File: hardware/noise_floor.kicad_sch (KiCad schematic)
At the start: 14 parts, among them J1 DC Power, J10 IO/Switch Connector 2 (Switch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, J11 Battery, J2 Input, J3 Output, J6 IO/Effect Connector 1 (IO Sid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, J7 IO/Switch Connector 1 (IO Sid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, J8 IO/Switch Connector 2 (IO Sid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, J9 IO/Switch Connector 1 (Switch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, SW1 Footswitch

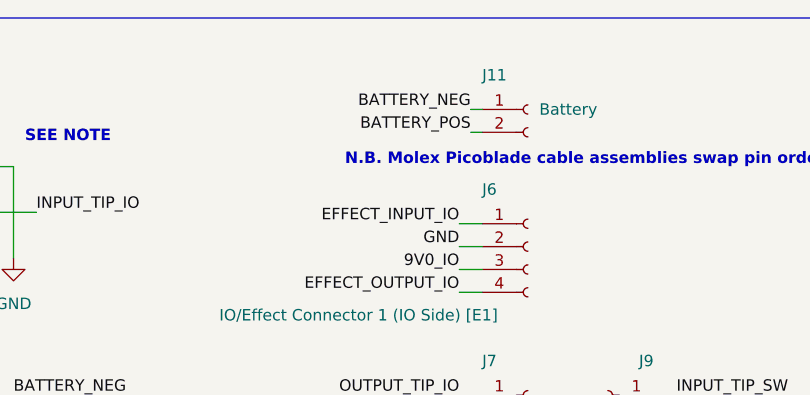
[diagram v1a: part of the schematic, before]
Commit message: Fix one issue discovered in testing of v0.2 hardware
 - swap nets on battery JST connector
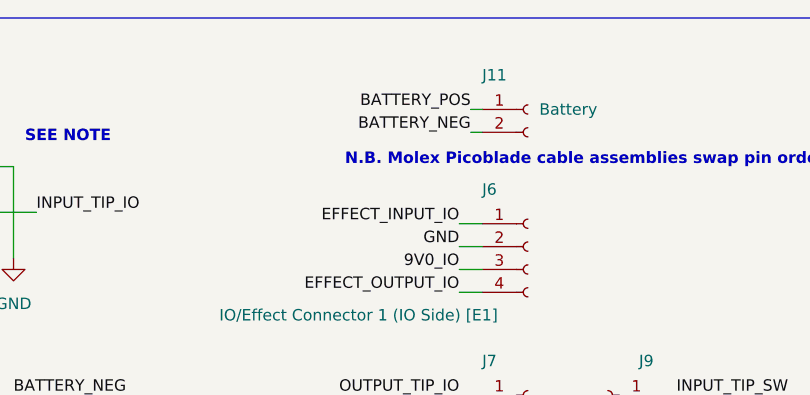
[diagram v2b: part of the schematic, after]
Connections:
- net BATTERY_NEG: now also J11.2 (Pin_2); no longer J11.1 (Pin_1)
- net BATTERY_POS: now also J11.1 (Pin_1); no longer J11.2 (Pin_2)
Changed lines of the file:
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@@
   (title_block
     (title "Noise Floor Interface Boards")
-    (date "2023-03-16")
-    (rev "v0.2")
+    (date "2023-03-23")
+    (rev "v0.21")
     (comment 1 "github.com/whbeers/noise_floor")
   )
@@
     (effects (font (size 1.27 1.27)) (justify left bottom))
   )
-  (label "BATTERY_POS" (at 85.09 26.67 180) (fields_autoplaced)
+  (label "BATTERY_NEG" (at 85.09 26.67 180) (fields_autoplaced)
     (effects (font (size 1.27 1.27)) (justify right bottom))
   )
-  (label "BATTERY_NEG" (at 85.09 24.13 180) (fields_autoplaced)
+  (label "BATTERY_POS" (at 85.09 24.13 180) (fields_autoplaced)
     (effects (font (size 1.27 1.27)) (justify right bottom))
   )

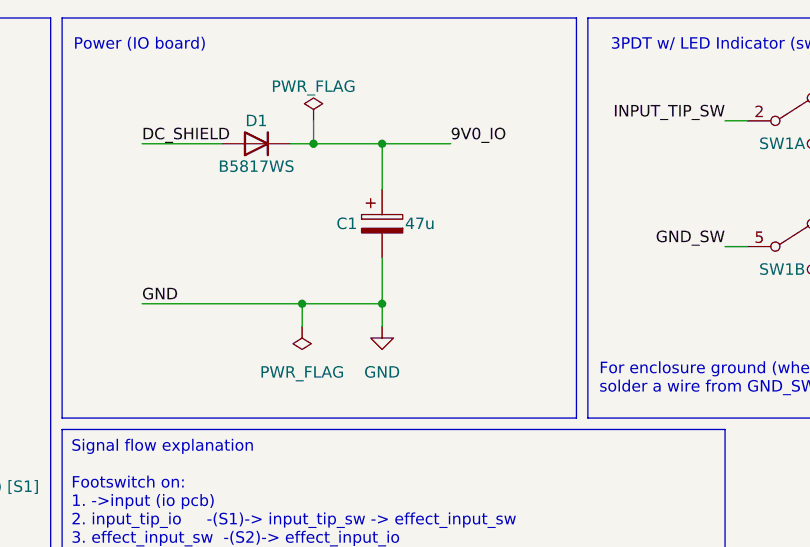
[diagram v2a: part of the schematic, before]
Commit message: improve power filtering and move to more SMD components
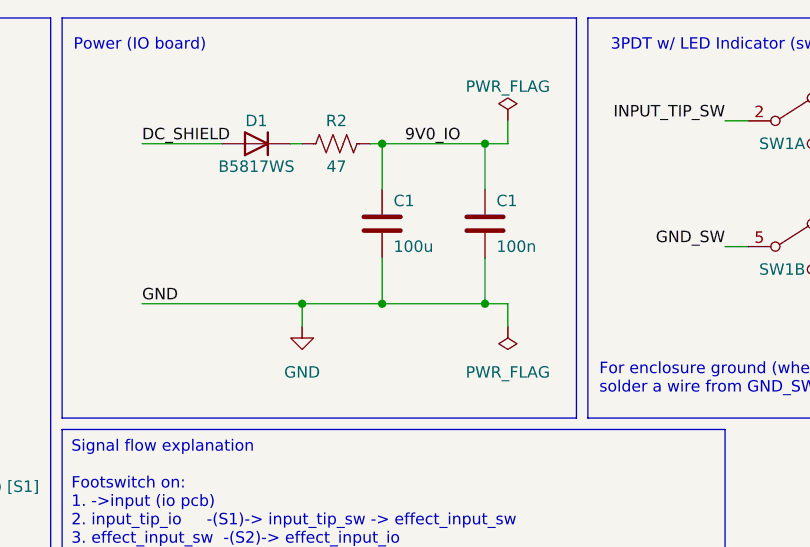
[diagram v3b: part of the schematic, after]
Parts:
- added C1: 100n, Capacitor_SMD:C_1206_3216Metric, symbol Device:C
- added R2: 47, Resistor_SMD:R_1206_3216Metric_Pad1.30x1.75mm_HandSolder, symbol Device:R_US
- C1: value 47u -> 100u; footprint Capacitor_THT:CP_Radial_D5.0mm_P2.50mm -> Capacitor_SMD:CP_Elec_6.3x7.7; symbol Device:C_Polarized -> Device:C
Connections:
- net 9V0_IO: now also C1.1, R2.1; no longer D1.1 (K)
- net GND: now also C1.2
- new net: D1.1 (K), R2.2

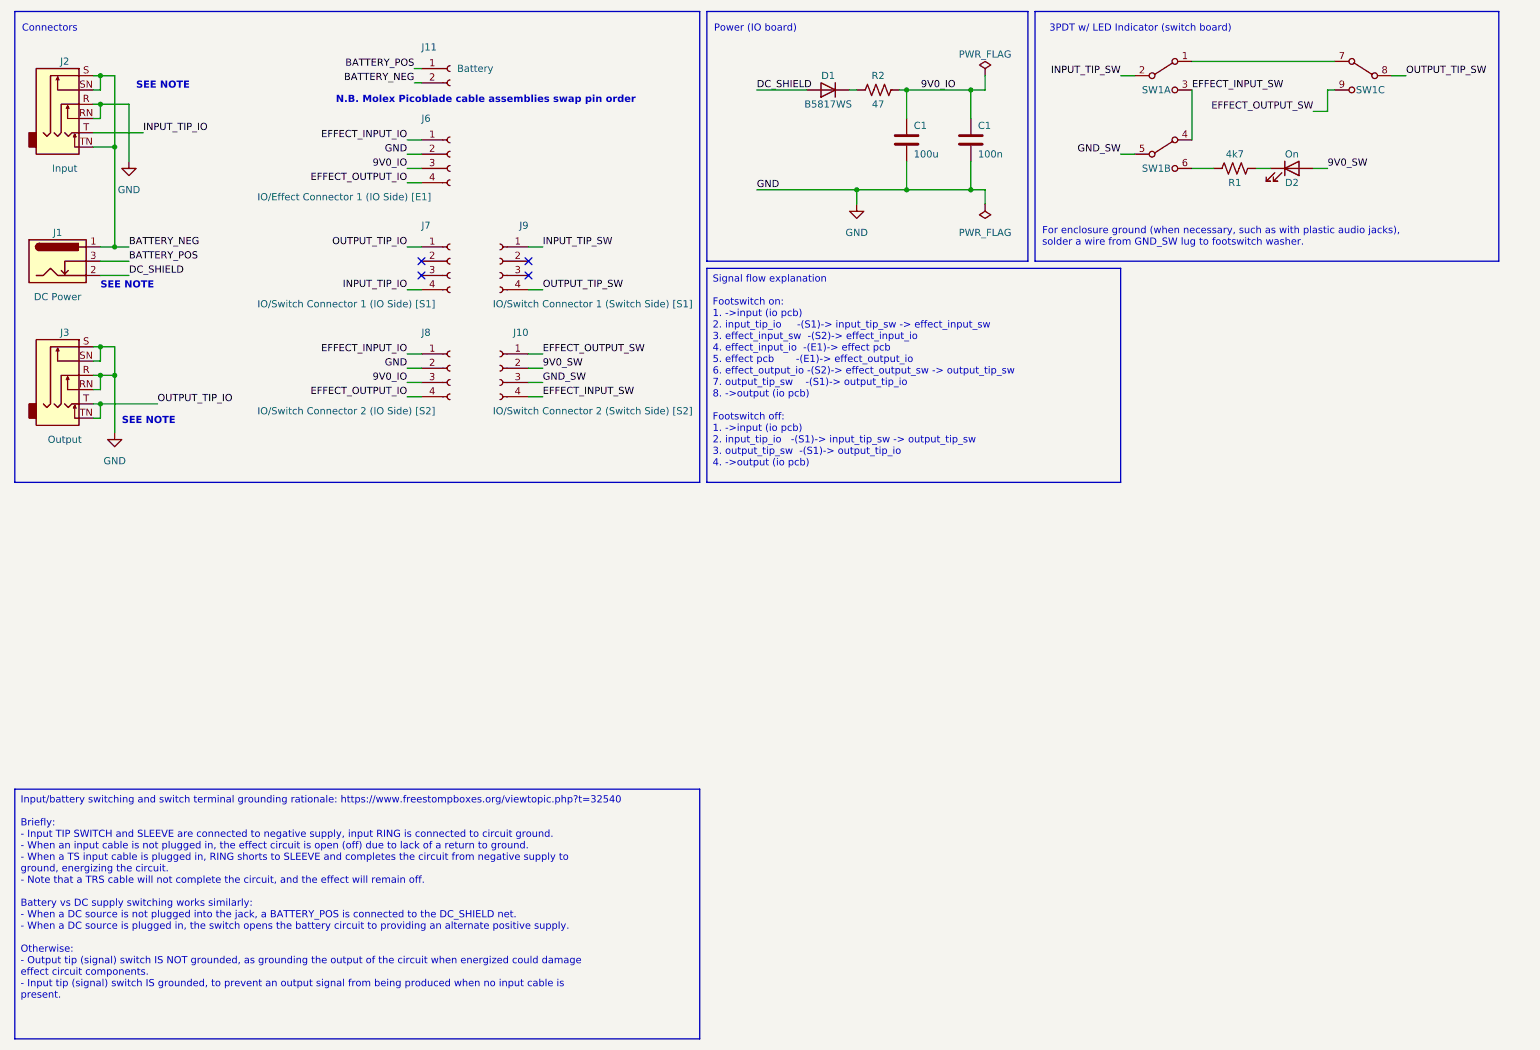
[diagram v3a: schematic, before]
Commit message: v0.30 includes a new "ux" board, with the initial feature set:
 - board-to-board connector interface for expandability
 - three potentiometers and three SPDT switches
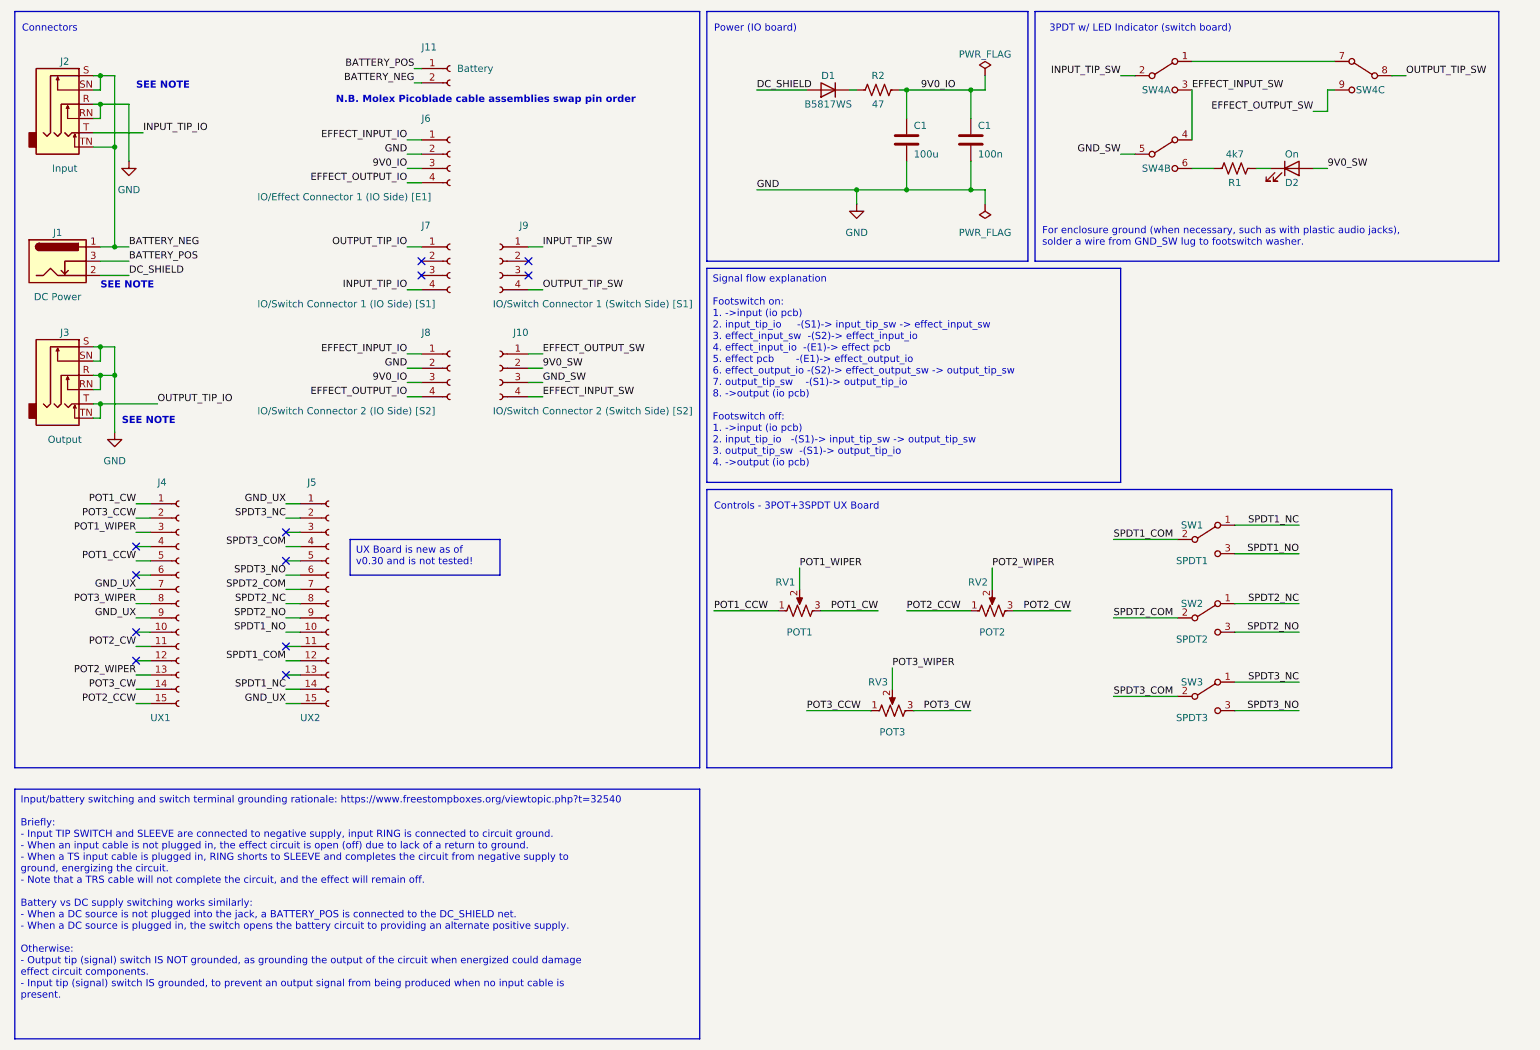
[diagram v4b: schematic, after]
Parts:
- added J4: UX1, noise_floor:Amphenol_Receptacle_15pin_10162581-3134115LF, symbol Connector:Conn_01x15_Socket
- added J5: UX2, noise_floor:Amphenol_Receptacle_15pin_10162581-3134115LF, symbol Connector:Conn_01x15_Socket
- added RV1: POT1, noise_floor:Potentiometer_Single_3_Horizontal, symbol Device:R_Potentiometer_US
- added RV2: POT2, noise_floor:Potentiometer_Single_3_Horizontal, symbol Device:R_Potentiometer_US
- added RV3: POT3, noise_floor:Potentiometer_Single_3_Horizontal, symbol Device:R_Potentiometer_US
- added SW1: SPDT1, noise_floor:SW_SPDT_SOLDER_LUGS, symbol Switch:SW_SPDT
- added SW2: SPDT2, noise_floor:SW_SPDT_SOLDER_LUGS, symbol Switch:SW_SPDT
- added SW3: SPDT3, noise_floor:SW_SPDT_SOLDER_LUGS, symbol Switch:SW_SPDT
- renumbered SW1 to SW4
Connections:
- new net GND_UX: J4.7 (Pin_7), J4.9 (Pin_9), J5.1 (Pin_1), J5.15 (Pin_15)
- new net POT1_CCW: J4.5 (Pin_5), RV1.1
- new net POT1_CW: J4.1 (Pin_1), RV1.3
- new net POT1_WIPER: J4.3 (Pin_3), RV1.2
- new net POT2_CCW: J4.15 (Pin_15), RV2.1
- new net POT2_CW: J4.11 (Pin_11), RV2.3
- new net POT2_WIPER: J4.13 (Pin_13), RV2.2
- new net POT3_CCW: J4.2 (Pin_2), RV3.1
- new net POT3_CW: J4.14 (Pin_14), RV3.3
- new net POT3_WIPER: J4.8 (Pin_8), RV3.2
- new net SPDT1_COM: J5.12 (Pin_12), SW1.2 (B)
- new net SPDT1_NC: J5.14 (Pin_14), SW1.1 (A)
- new net SPDT1_NO: J5.10 (Pin_10), SW1.3 (C)
- new net SPDT2_COM: J5.7 (Pin_7), SW2.2 (B)
- new net SPDT2_NC: J5.8 (Pin_8), SW2.1 (A)
- new net SPDT2_NO: J5.9 (Pin_9), SW2.3 (C)
- new net SPDT3_COM: J5.4 (Pin_4), SW3.2 (B)
- new net SPDT3_NC: J5.2 (Pin_2), SW3.1 (A)
- new net SPDT3_NO: J5.6 (Pin_6), SW3.3 (C)
- no-connect marks 4 -> 12
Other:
- note added: "Controls - 3POT+3SPDT UX Board"

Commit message: Add pot adjustment resistors, adapt to different layout and reroute, bump to v0.31
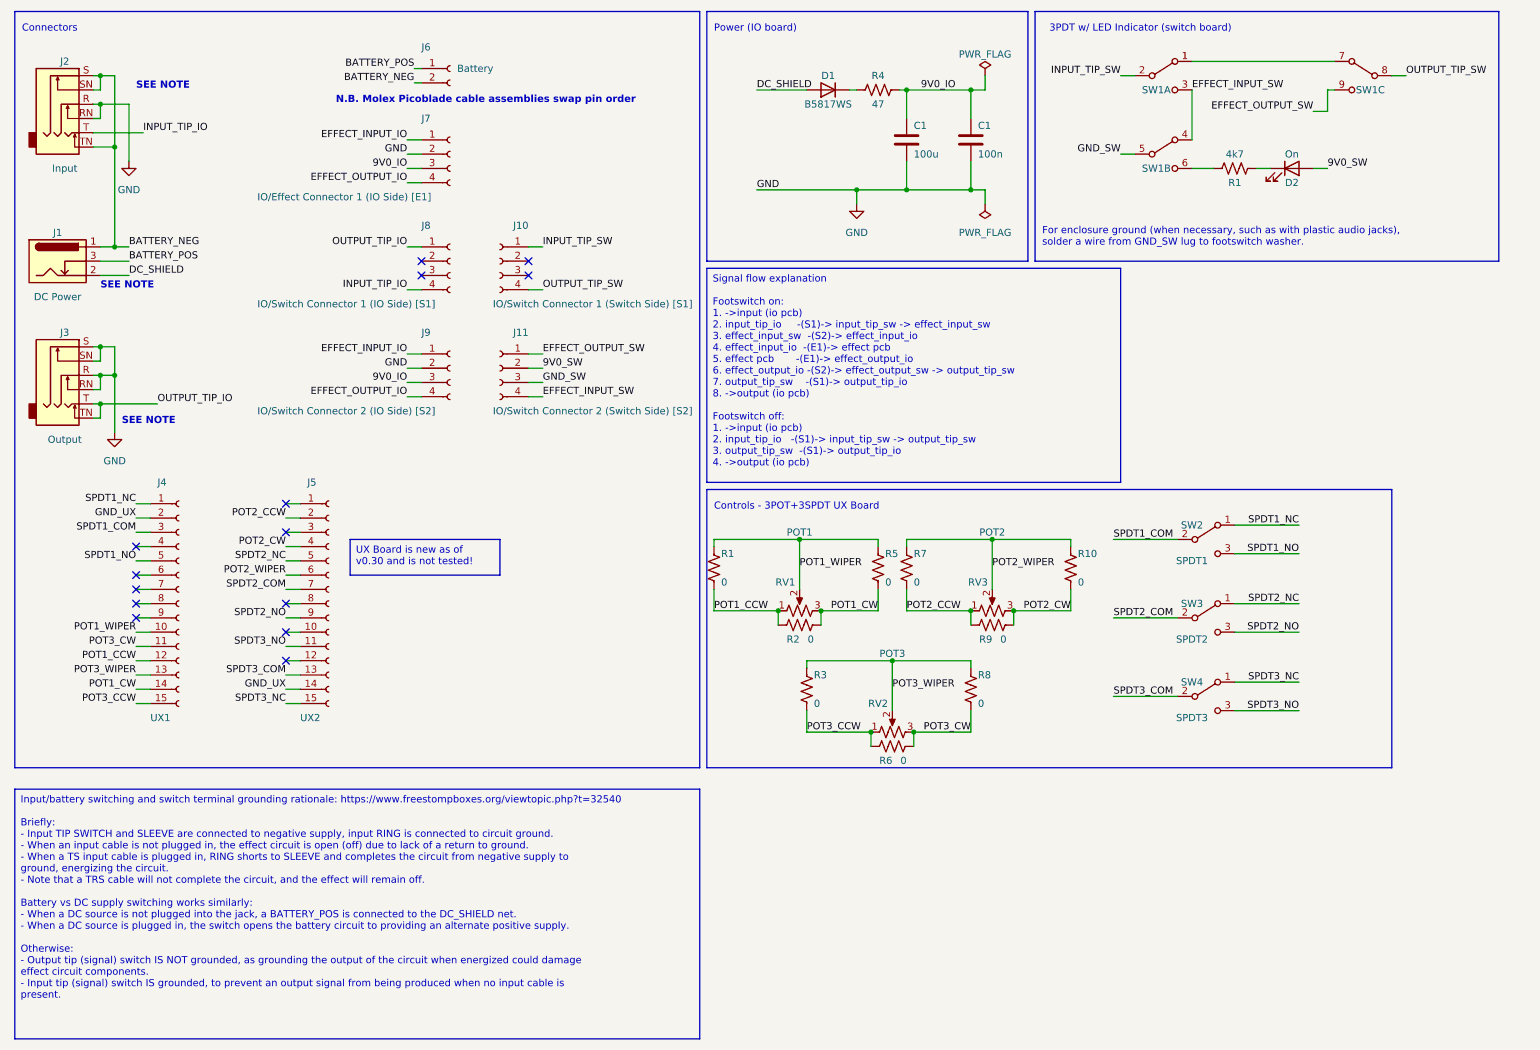
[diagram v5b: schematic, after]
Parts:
- added R1, R10, R2, R3, R5, R6, R7, R8, R9: 0, Resistor_THT:R_Axial_DIN0207_L6.3mm_D2.5mm_P7.62mm_Horizontal, symbol Device:R_US
- renumbered J9 to J10, J10 to J11, J11 to J6, J6 to J7, J7 to J8, J8 to J9, R2 to R4, RV3 to RV2, RV2 to RV3, SW4 to SW1, SW1 to SW2, SW2 to SW3, SW3 to SW4
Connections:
- net GND_UX: now also J4.2 (Pin_2), J5.14 (Pin_14); no longer J4.7 (Pin_7), J4.9 (Pin_9), J5.1 (Pin_1), J5.15 (Pin_15)
- net POT1_CCW: now also J4.12 (Pin_12), R1.1, R2.2; no longer J4.5 (Pin_5)
- net POT1_CW: now also J4.14 (Pin_14), R2.1, R5.1; no longer J4.1 (Pin_1)
- net POT1_WIPER: now also J4.10 (Pin_10), R1.2, R5.2; no longer J4.3 (Pin_3)
- net POT2_CCW: now also J5.2 (Pin_2), R7.1, R9.2; no longer J4.15 (Pin_15)
- net POT2_CW: now also J5.4 (Pin_4), R10.1, R9.1; no longer J4.11 (Pin_11)
- net POT2_WIPER: now also J5.6 (Pin_6), R10.2, R7.2; no longer J4.13 (Pin_13)
- net POT3_CCW: now also J4.15 (Pin_15), R3.1, R6.2; no longer J4.2 (Pin_2)
- net POT3_CW: now also J4.11 (Pin_11), R6.1, R8.1; no longer J4.14 (Pin_14)
- net POT3_WIPER: now also J4.13 (Pin_13), R3.2, R8.2; no longer J4.8 (Pin_8)
- net SPDT1_COM: now also J4.3 (Pin_3); no longer J5.12 (Pin_12)
- net SPDT1_NC: now also J4.1 (Pin_1); no longer J5.14 (Pin_14)
- net SPDT1_NO: now also J4.5 (Pin_5); no longer J5.10 (Pin_10)
- net SPDT2_NC: now also J5.5 (Pin_5); no longer J5.8 (Pin_8)
- net SPDT3_COM: now also J5.13 (Pin_13); no longer J5.4 (Pin_4)
- net SPDT3_NC: now also J5.15 (Pin_15); no longer J5.2 (Pin_2)
- net SPDT3_NO: now also J5.11 (Pin_11); no longer J5.6 (Pin_6)
- no-connect marks 12 -> 14
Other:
- moved on the sheet: RV2
